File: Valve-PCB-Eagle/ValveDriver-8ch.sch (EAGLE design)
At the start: 29 parts, among them IC1 ULQ2803A, J10 Valve 3, J11 Valve 2, J12 Valve 1, J15 BNCPTH, J16 BNCPTH, J17 BNCPTH, J18 BNCPTH, J4 POWER_JACK, J5 Valve 8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

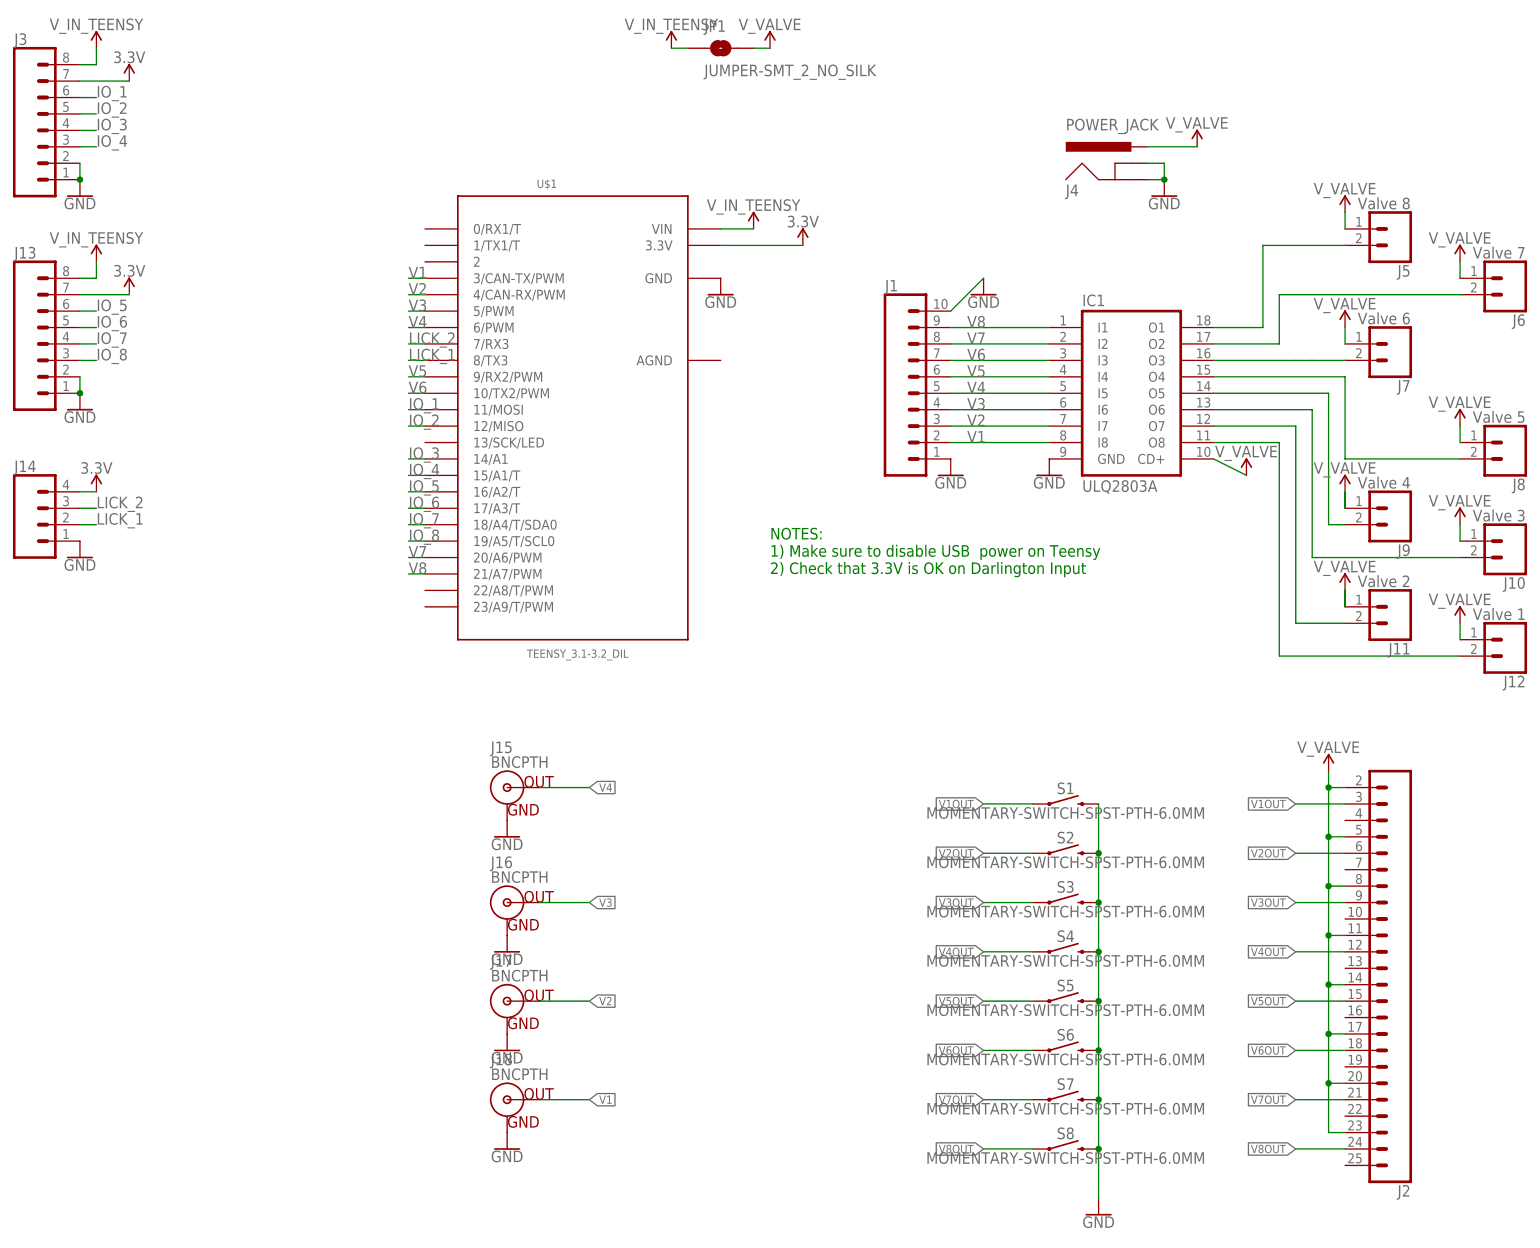
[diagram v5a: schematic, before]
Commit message: [Valve] Remove manifold; remove buttons 5–8; make PCB more compact
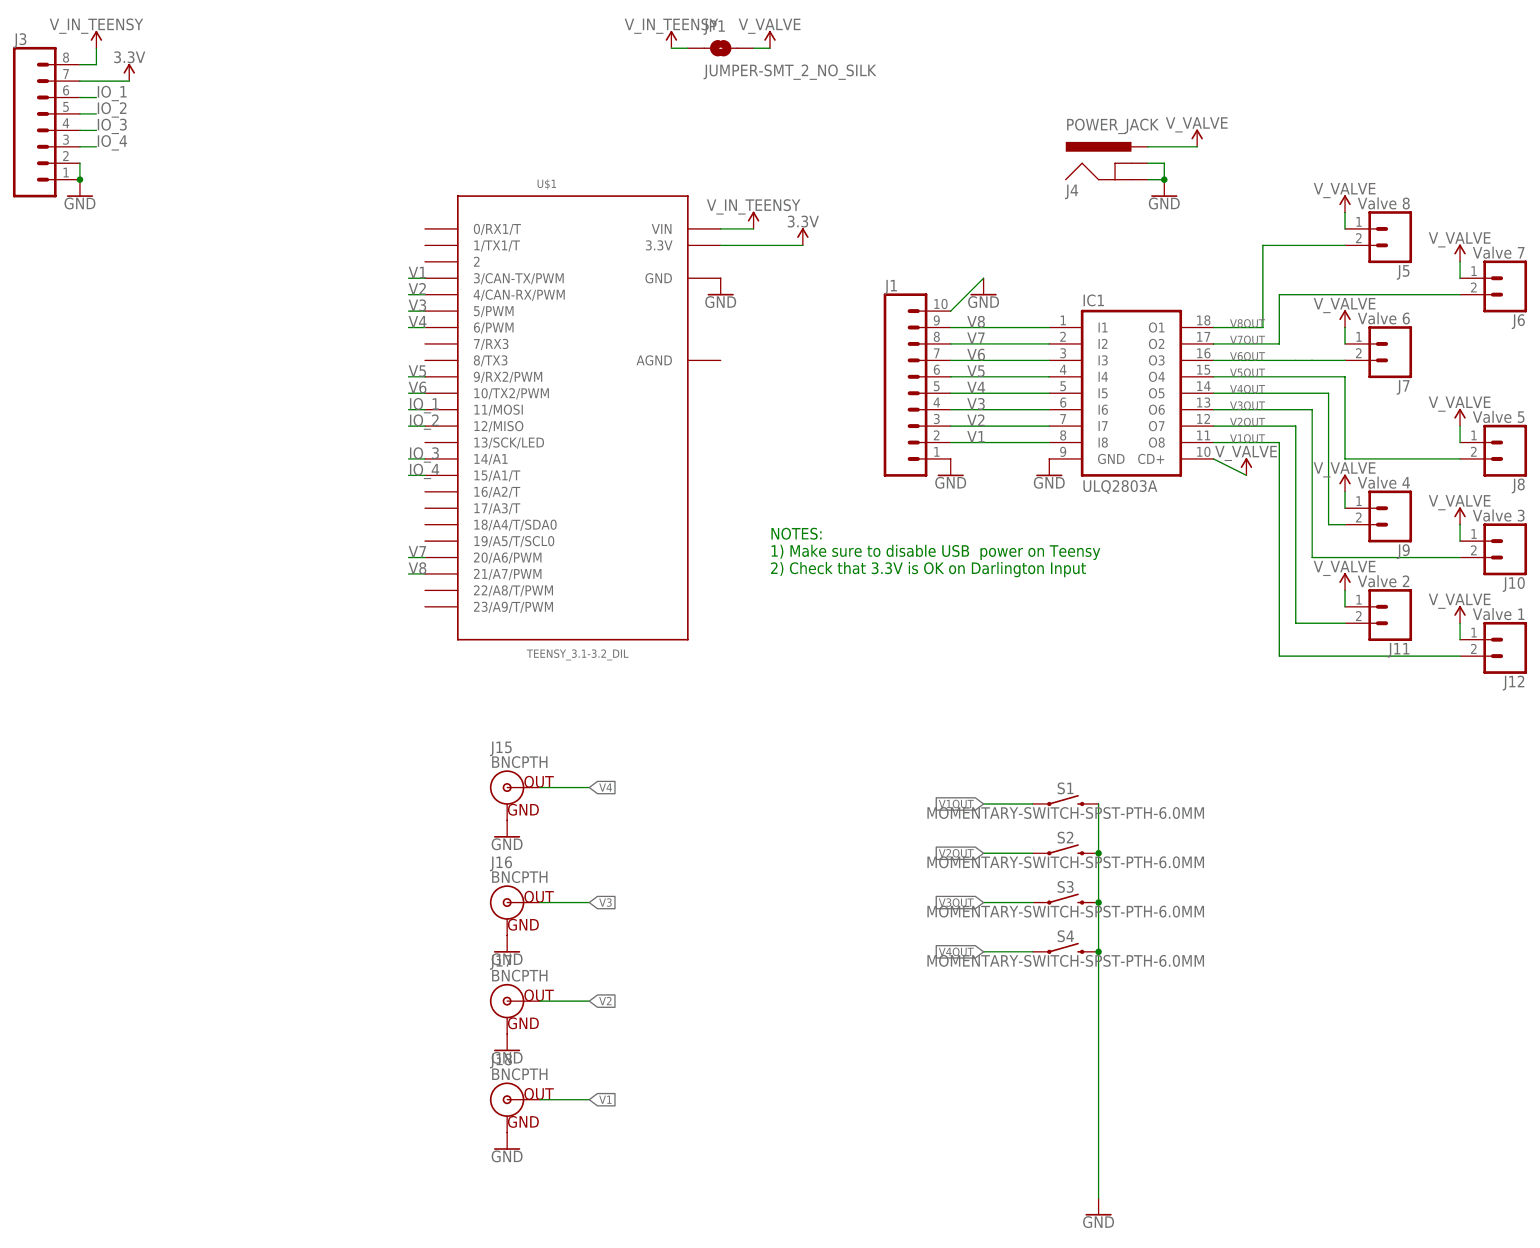
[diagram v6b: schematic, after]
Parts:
- removed J13: (no value), SparkFun-Connectors:CONN_083.5MM-8
- removed J14: (no value), SparkFun-Connectors:CONN_04
- removed J2: (no value), SparkFun-Connectors:CONN_24
- removed S5, S6, S7, S8: MOMENTARY-SWITCH-SPST-PTH-6.0MM, SparkFun-Switches:MOMENTARY-SWITCH-SPST-PTH-6.0MM
- J3: device SparkFun-Connectors:CONN_083.5MM-8 -> SparkFun-Connectors:CONN_08"
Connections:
- removed net IO_5: J13.6, U$1.16/A2/T
- removed net IO_6: J13.5, U$1.17/A3/T
- removed net IO_7: J13.4, U$1.18/A4/T/SDA0
- removed net IO_8: J13.3, U$1.19/A5/T/SCL0
- removed net LICK_1: J14.2, U$1.8/TX3
- removed net LICK_2: J14.3, U$1.7/RX3
- net 3.3V: no longer J13.7, J14.4
- net GND: no longer J13.1, J13.2, J14.1, S5.2, S6.2, S7.2, S8.2
- net V1OUT: no longer J2.3
- net V2OUT: no longer J2.6
- net V3OUT: no longer J2.9
- net V4OUT: no longer J2.12
- net V5OUT: no longer J2.15, S5.1
- net V6OUT: no longer J2.18, S6.1
- net V7OUT: no longer J2.21, S7.1
- net V8OUT: no longer J2.24, S8.1
- net V_IN_TEENSY: no longer J13.8
- net V_VALVE: no longer J2.11, J2.14, J2.17, J2.2, J2.20, J2.23, J2.5, J2.8

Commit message: [Valve] Removed Teensy and associated I/O connections
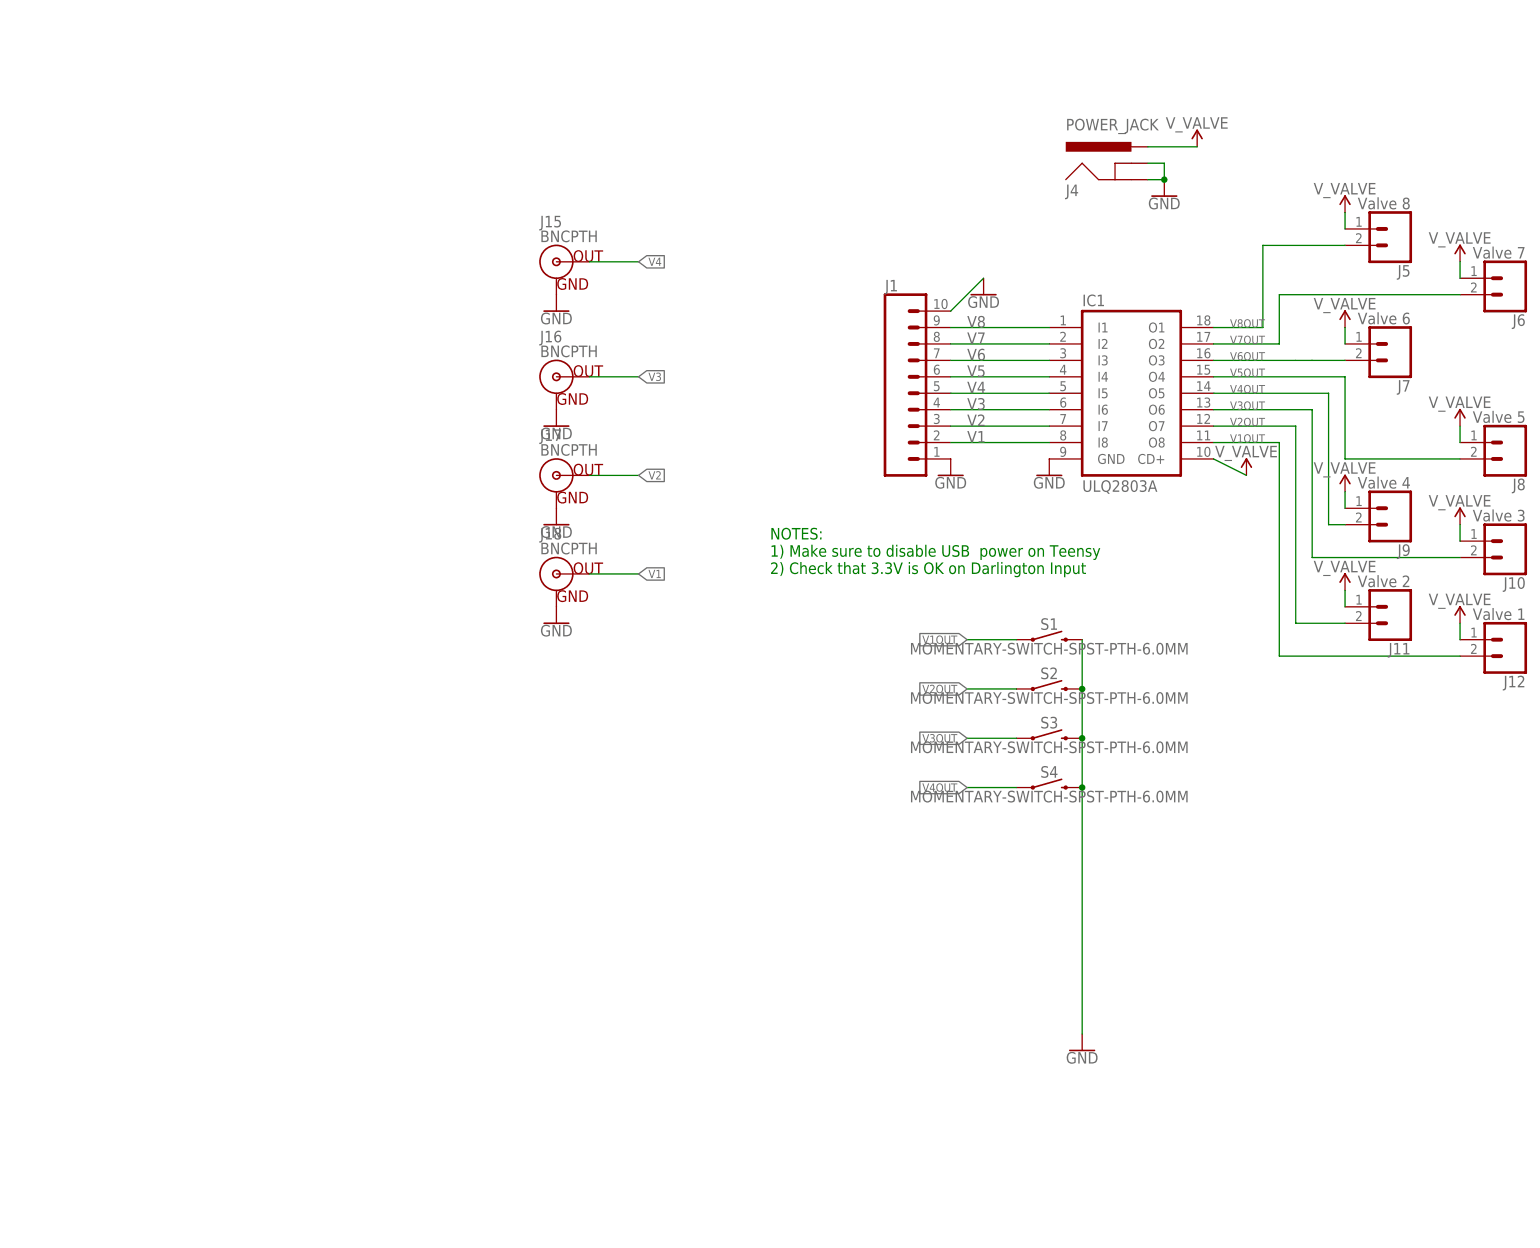
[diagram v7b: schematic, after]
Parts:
- removed J3: (no value), SparkFun-Connectors:CONN_08"
- removed JP1: JUMPER-SMT_2_NO_SILK, SparkFun-Jumpers:JUMPER-SMT_2_NO_SILK
- removed U$1: TEENSY_3.1-3.2_DIL, Teensy_3_and_LC_Series_Boards_v1.4:TEENSY_3.1-3.2_DIL
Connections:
- removed net 3.3V: J3.7, U$1.3.3V
- removed net IO_1: J3.6, U$1.11/MOSI
- removed net IO_2: J3.5, U$1.12/MISO
- removed net IO_3: J3.4, U$1.14/A1
- removed net IO_4: J3.3, U$1.15/A1/T
- removed net V_IN_TEENSY: J3.8, JP1.1, U$1.VIN
- net GND: no longer J3.1, J3.2, U$1.GND
- net V1: no longer U$1.3/CAN-TX/PWM
- net V2: no longer U$1.4/CAN-RX/PWM
- net V3: no longer U$1.5/PWM
- net V4: no longer U$1.6/PWM
- net V5: no longer U$1.9/RX2/PWM
- net V6: no longer U$1.10/TX2/PWM
- net V7: no longer U$1.20/A6/PWM
- net V8: no longer U$1.21/A7/PWM
- net V_VALVE: no longer JP1.2
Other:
- moved on the sheet: J15, J16, J17, J18, S1, S2, S3, S4
